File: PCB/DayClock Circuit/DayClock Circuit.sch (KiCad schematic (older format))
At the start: 42 parts, among them J10 Conn_02x08_Odd_Even, J11 Conn_01x02, J12 Conn_01x03, J13 Conn_01x03, J14 Stepper Motor, J3 molex 15-24-4441, J5 4002 LCD Screen, J6 Encoder, J7 RGB_LED_Strip_Connector, J8 RGB_LED_Strip_Connector, J9 RGB_LED_Strip_Connector, Q1 N-MOSFET, Q2 N-MOSFET, Q3 N-MOSFET, Q4 N-MOSFET, Q5 N-MOSFET, Q6 N-MOSFET, Q7 N-MOSFET, Q8 N-MOSFET, Q9 N-MOSFET, SW1 SW_DIP_x03, U1 Tiny_RTC_DS1307, U2 DRV8825_module

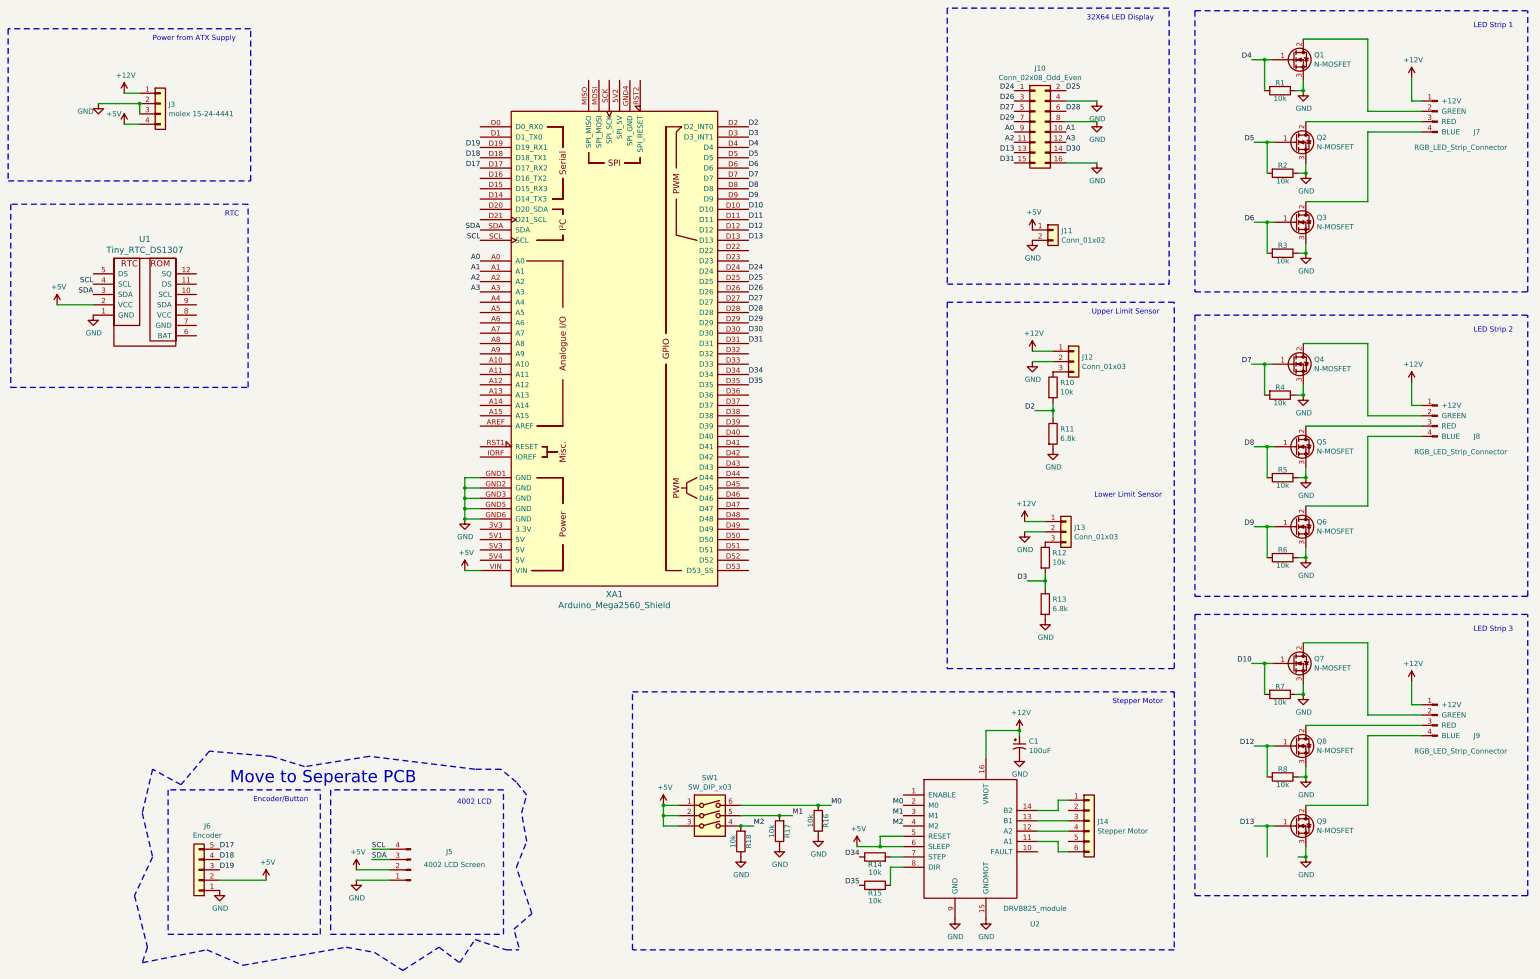
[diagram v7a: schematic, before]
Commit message: Split control box to a seperate PCB connected by a CAT5 cable. Schematic is complete, foot prints need to be finalized before layout.
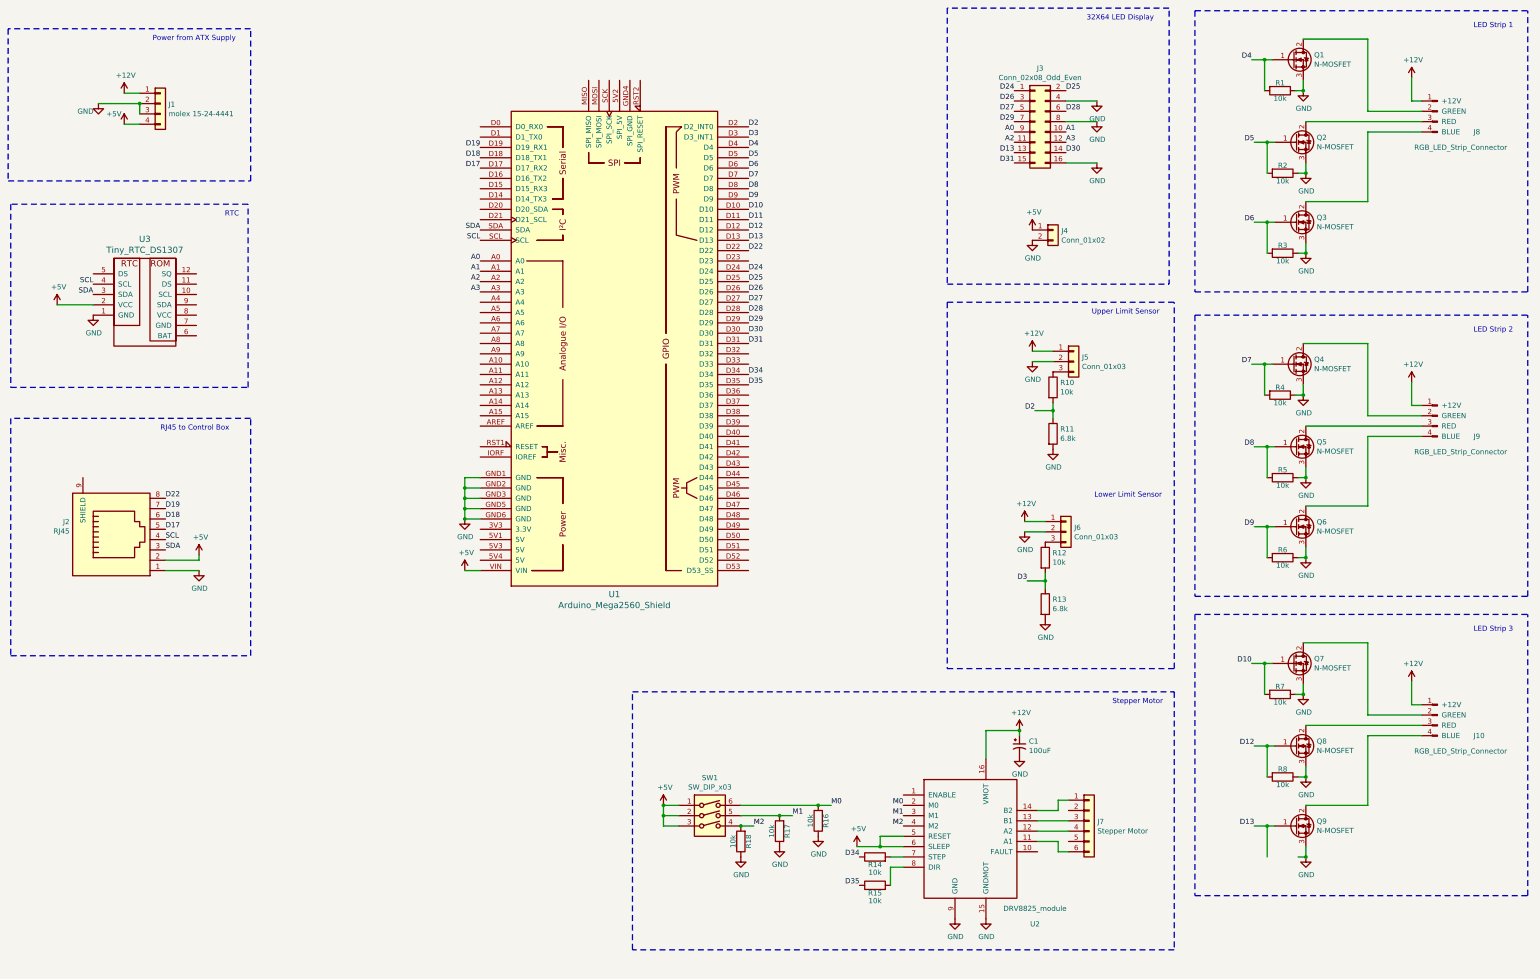
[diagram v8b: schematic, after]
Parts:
- removed J5: 4002 LCD Screen, Connectors_JST:JST_XH_B04B-XH-A_04x2.50mm_Straight, symbol Connector_Generic:Conn_01x04_Male
- removed J6: Encoder, Connector_JST:JST_XH_B05B-XH-A_1x05_P2.50mm_Vertical, symbol Connector_Generic:Conn_01x05
- added J2: RJ45, Connector_RJ:RJ45_Amphenol_RJHSE538X, symbol Connector_Specialized:RJ45
- C1: footprint (none) -> Capacitor_THT:CP_Radial_D6.3mm_P2.50mm
- renumbered J3 to J1, J9 to J10, J10 to J3, J11 to J4, J12 to J5, J13 to J6, J14 to J7, J7 to J8, J8 to J9, XA1 to U1, U1 to U3
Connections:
- net +5V: now also J2.2
- net D17: now also J2.5
- net D18: now also J2.6
- net D19: now also J2.7
- net GND: now also J2.1
- net SCL: now also J2.4
- net SDA: now also J2.3
- net D22: now reaches U1.D22
- net D22: now also J2.8
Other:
- note added: "RJ45 to Control Box"
- note removed: "4002 LCD"
- note removed: "Encoder/Button"
- note removed: "Move to Seperate PCB"
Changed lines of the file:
@@
 $EndDescr
 $Comp
-L rich_symbols:Tiny_RTC_DS1307 U1
+L rich_symbols:Tiny_RTC_DS1307 U3
 U 1 1 5A71AFB0
 P 2350 3625
-F 0 "U1" H 2350 4312 60  0000 C CNN
+F 0 "U3" H 2350 4312 60  0000 C CNN
 F 1 "Tiny_RTC_DS1307" H 2350 4206 60  0000 C CNN
 F 2 "rich-footprints:TinyRTC-one-mounting-hole" H 2400 3725 60  0001 C CNN
@@
 	1    0    0    -1
 $EndComp
-Text Label 4550 8850 0    50   ~ 0
-SCL
-Text Label 4550 8950 0    50   ~ 0
-SDA
-Wire Wire Line
-	4550 8850 4725 8850
-Wire Wire Line
-	4550 8950 4725 8950
 $Comp
 L power:+5V #PWR09
@@
 	1850 3575 1500 3575
 $Comp
-L power:GND #PWR013
-U 1 1 5A79A6E1
-P 3075 9250
-F 0 "#PWR013" H 3075 9000 50  0001 C CNN
-F 1 "GND" H 3080 9077 50  0000 C CNN
-F 2 "" H 3075 9250 50  0001 C CNN
-F 3 "" H 3075 9250 50  0001 C CNN
-	1    3075 9250
-	1    0    0    -1
-$EndComp
-$Comp
-L Connector_Generic:Conn_01x04_Male J5
-U 1 1 5AFFD786
-P 4925 9050
-F 0 "J5" H 4550 8875 50  0000 C CNN
-F 1 "4002 LCD Screen" H 4500 9000 50  0000 C CNN
-F 2 "Connectors_JST:JST_XH_B04B-XH-A_04x2.50mm_Straight" H 4925 9050 50  0001 C CNN
-F 3 "~" H 4925 9050 50  0001 C CNN
-	1    4925 9050
-	-1   0    0    1
-$EndComp
-$Comp
-L power:+5V #PWR0101
-U 1 1 5AFFEF10
-P 4400 9050
-F 0 "#PWR0101" H 4400 8900 50  0001 C CNN
-F 1 "+5V" H 4415 9223 50  0000 C CNN
-F 2 "" H 4400 9050 50  0001 C CNN
-F 3 "" H 4400 9050 50  0001 C CNN
-	1    4400 9050
-	1    0    0    -1
-$EndComp
-$Comp
-L power:GND #PWR0102
-U 1 1 5AFFEF2B
-P 4400 9150
-F 0 "#PWR0102" H 4400 8900 50  0001 C CNN
-F 1 "GND" H 4405 8977 50  0000 C CNN
-F 2 "" H 4400 9150 50  0001 C CNN
-F 3 "" H 4400 9150 50  0001 C CNN
-	1    4400 9150
-	1    0    0    -1
-$EndComp
-Wire Wire Line
-	4725 9150 4400 9150
-Wire Wire Line
-	4400 9050 4725 9050
-$Comp
-L Connector_Generic:Conn_01x05 J6
-U 1 1 5B03D90E
-P 2875 9050
-F 0 "J6" H 2795 8625 50  0000 C CNN
-F 1 "Encoder" H 2795 8716 50  0000 C CNN
-F 2 "Connector_JST:JST_XH_B05B-XH-A_1x05_P2.50mm_Vertical" H 2875 9050 50  0001 C CNN
-F 3 "~" H 2875 9050 50  0001 C CNN
-	1    2875 9050
-	-1   0    0    1
-$EndComp
-$Comp
-L power:+5V #PWR0103
-U 1 1 5B03DD9C
-P 3525 9150
-F 0 "#PWR0103" H 3525 9000 50  0001 C CNN
-F 1 "+5V" H 3540 9323 50  0000 C CNN
-F 2 "" H 3525 9150 50  0001 C CNN
-F 3 "" H 3525 9150 50  0001 C CNN
-	1    3525 9150
-	1    0    0    -1
-$EndComp
-Wire Wire Line
-	3075 9150 3525 9150
-$Comp
-L rich_symbols:RGB_LED_Strip_Connector J7
+L rich_symbols:RGB_LED_Strip_Connector J8
 U 1 1 5B09E233
 P 14825 1750
-F 0 "J7" H 15225 1600 50  0000 L CNN
+F 0 "J8" H 15225 1600 50  0000 L CNN
 F 1 "RGB_LED_Strip_Connector" H 14650 1450 50  0000 L CNN
 F 2 "Connector_JST:JST_XH_B04B-XH-A_1x04_P2.50mm_Vertical" H 14825 1750 50  0001 C CNN
@@
 LED Strip 1
 $Comp
-L rich_symbols:RGB_LED_Strip_Connector J8
+L rich_symbols:RGB_LED_Strip_Connector J9
 U 1 1 5B0C5230
 P 14825 4700
-F 0 "J8" H 15225 4550 50  0000 L CNN
+F 0 "J9" H 15225 4550 50  0000 L CNN
 F 1 "RGB_LED_Strip_Connector" H 14650 4400 50  0000 L CNN
 F 2 "Connector_JST:JST_XH_B04B-XH-A_1x04_P2.50mm_Vertical" H 14825 4700 50  0001 C CNN
@@
 LED Strip 2
 $Comp
-L rich_symbols:RGB_LED_Strip_Connector J9
+L rich_symbols:RGB_LED_Strip_Connector J10
 U 1 1 5B0C699D
 P 14825 7600
-F 0 "J9" H 15225 7450 50  0000 L CNN
+F 0 "J10" H 15225 7450 50  0000 L CNN
 F 1 "RGB_LED_Strip_Connector" H 14650 7300 50  0000 L CNN
 F 2 "Connector_JST:JST_XH_B04B-XH-A_1x04_P2.50mm_Vertical" H 14825 7600 50  0001 C CNN
@@
 LED Strip 3
 $Comp
-L Connector_Generic:Conn_02x08_Odd_Even J10
+L Connector_Generic:Conn_02x08_Odd_Even J3
 U 1 1 5B0E4FF2
 P 10975 1800
-F 0 "J10" H 11025 2317 50  0000 C CNN
+F 0 "J3" H 11025 2317 50  0000 C CNN
 F 1 "Conn_02x08_Odd_Even" H 11025 2226 50  0000 C CNN
 F 2 "Connector_PinHeader_2.54mm:PinHeader_2x08_P2.54mm_Vertical" H 10975 1800 50  0001 C CNN
@@
 	10125 3375 12275 3375
 $Comp
-L arduino:Arduino_Mega2560_Shield XA1
+L arduino:Arduino_Mega2560_Shield U1
 U 1 1 5B0E5F76
 P 6900 4000
-F 0 "XA1" H 6900 1620 60  0000 C CNN
+F 0 "U1" H 6900 1620 60  0000 C CNN
 F 1 "Arduino_Mega2560_Shield" H 6900 1514 60  0000 C CNN
 F 2 "Arduino:Arduino_Mega2560_Shield" H 7600 6750 60  0001 C CNN
@@
 $EndComp
 $Comp
-L Connector_Generic:Conn_01x02 J11
+L Connector_Generic:Conn_01x02 J4
 U 1 1 5B0E97EB
 P 11150 2850
-F 0 "J11" H 11230 2842 50  0000 L CNN
+F 0 "J4" H 11230 2842 50  0000 L CNN
 F 1 "Conn_01x02" H 11230 2751 50  0000 L CNN
 F 2 "TerminalBlock:TerminalBlock_Altech_AK300-2_P5.00mm" H 11150 2850 50  0001 C CNN
@@
 RTC
 $Comp
-L Connector_Generic:Conn_01x04 J3
+L Connector_Generic:Conn_01x04 J1
 U 1 1 5B13490E
 P 2500 1625
-F 0 "J3" H 2579 1617 50  0000 L CNN
+F 0 "J1" H 2579 1617 50  0000 L CNN
 F 1 "molex 15-24-4441" H 2579 1526 50  0000 L CNN
 F 2 "TerminalBlock_Phoenix:TerminalBlock_Phoenix_MKDS-1,5-4-5.08_1x04_P5.08mm_Horizontal" H 2500 1625 50  0001 C CNN
@@
 Text Notes 2425 1025 0    50   ~ 0
 Power from ATX Supply
-Wire Notes Line
-	5825 9675 5825 8275
-Wire Notes Line
-	5825 8275 4150 8275
-Wire Notes Line
-	4150 8275 4150 9675
-Wire Notes Line
-	4150 9675 5825 9675
-Text Notes 5375 8425 0    50   ~ 0
-4002 LCD
-Wire Notes Line
-	4050 9675 4050 8275
-Wire Notes Line
-	4050 8275 2575 8275
-Wire Notes Line
-	2575 8275 2575 9675
-Wire Notes Line
-	2575 9675 4050 9675
-Text Notes 3400 8400 0    50   ~ 0
-Encoder/Button
-Wire Notes Line
-	5975 9800 5925 9625
-Wire Notes Line
-	5925 9625 6100 9475
-Wire Notes Line
-	6100 9475 5950 9025
-Wire Notes Line
-	5950 9025 6050 8775
-Wire Notes Line
-	6050 8775 6000 8500
-Wire Notes Line
-	6000 8500 6050 8325
-Wire Notes Line
-	6050 8325 5950 8200
-Wire Notes Line
-	5950 8200 5800 8075
-Wire Notes Line
-	5800 8075 5550 8075
-Wire Notes Line
-	5550 8075 4525 7950
-Wire Notes Line
-	4525 7950 3900 8050
-Wire Notes Line
-	3575 7950 2975 7900
-Wire Notes Line
-	2975 7900 2700 8225
-Wire Notes Line
-	2700 8225 2425 8075
-Wire Notes Line
-	2425 8075 2325 8500
-Wire Notes Line
-	2325 8500 2425 8925
-Wire Notes Line
-	2425 8925 2250 9300
-Wire Notes Line
-	2250 9300 2375 9800
-Wire Notes Line
-	2375 9800 2325 9950
-Wire Notes Line
-	2325 9950 2950 9825
-Wire Notes Line
-	2950 9825 3300 9975
-Wire Notes Line
-	3300 9975 4300 9800
-Wire Notes Line
-	4300 9800 4575 9850
-Wire Notes Line
-	4575 9850 4850 10025
-Wire Notes Line
-	4850 10025 5200 9800
-Wire Notes Line
-	5200 9800 5400 9950
-Wire Notes Line
-	5400 9950 5550 9725
-Wire Notes Line
-	5550 9725 5850 9825
-Wire Notes Line
-	5850 9825 5975 9825
-Text Notes 3175 8225 0    118  ~ 0
-Move to Seperate PCB
-Wire Notes Line
-	3575 7950 3900 8050
-Text Label 3075 8850 0    50   ~ 0
+Text Label 2550 5750 0    50   ~ 0
 D17
-Text Label 3075 8950 0    50   ~ 0
+Text Label 2550 5650 0    50   ~ 0
 D18
-Text Label 3075 9050 0    50   ~ 0
+Text Label 2550 5550 0    50   ~ 0
 D19
 Text Label 5600 2250 2    50   ~ 0
@@
 D19
 $Comp
-L Connector_Generic:Conn_01x03 J12
+L Connector_Generic:Conn_01x03 J5
 U 1 1 5B10F747
 P 11350 4125
-F 0 "J12" H 11430 4167 50  0000 L CNN
+F 0 "J5" H 11430 4167 50  0000 L CNN
 F 1 "Conn_01x03" H 11430 4076 50  0000 L CNN
 F 2 "Connector_JST:JST_XH_B03B-XH-A_1x03_P2.50mm_Vertical" H 11350 4125 50  0001 C CNN
@@
 Upper Limit Sensor
 $Comp
-L Connector_Generic:Conn_01x03 J13
+L Connector_Generic:Conn_01x03 J6
 U 1 1 5B14EA09
 P 11275 5775
-F 0 "J13" H 11355 5817 50  0000 L CNN
+F 0 "J6" H 11355 5817 50  0000 L CNN
 F 1 "Conn_01x03" H 11355 5726 50  0000 L CNN
 F 2 "Connector_JST:JST_XH_B03B-XH-A_1x03_P2.50mm_Vertical" H 11275 5775 50  0001 C CNN
@@
 $EndComp
 $Comp
-L Connector_Generic:Conn_01x06 J14
+L Connector_Generic:Conn_01x06 J7
 U 1 1 5B169A57
 P 11500 8575
-F 0 "J14" H 11580 8567 50  0000 L CNN
+F 0 "J7" H 11580 8567 50  0000 L CNN
 F 1 "Stepper Motor" H 11580 8476 50  0000 L CNN
 F 2 "" H 11500 8575 50  0001 C CNN
@@
 F 0 "C1" H 10916 7896 50  0000 L CNN
 F 1 "100uF" H 10916 7805 50  0000 L CNN
-F 2 "" H 10825 7850 50  0001 C CNN
+F 2 "Capacitor_THT:CP_Radial_D6.3mm_P2.50mm" H 10825 7850 50  0001 C CNN
 F 3 "~" H 10825 7850 50  0001 C CNN
 	1    10825 7850
@@
 Wire Wire Line
 	9575 9025 9575 9200
+$Comp
+L Connector_Specialized:RJ45 J2
+U 1 1 5B12B8C7
+P 2100 5800
+F 0 "J2" V 2223 6280 50  0000 L CNN
+F 1 "RJ45" V 2132 6280 50  0000 L CNN
+F 2 "Connector_RJ:RJ45_Amphenol_RJHSE538X" H 2100 5800 50  0001 C CNN
+F 3 "" H 2100 5800 50  0001 C CNN
+	1    2100 5800
+	0    -1   -1   0
+$EndComp
+$Comp
+L power:GND #PWR0101
+U 1 1 5B145465
+P 2875 6150
+F 0 "#PWR0101" H 2875 5900 50  0001 C CNN
+F 1 "GND" H 2880 5977 50  0000 C CNN
+F 2 "" H 2875 6150 50  0001 C CNN
+F 3 "" H 2875 6150 50  0001 C CNN
+	1    2875 6150
+	1    0    0    -1
+$EndComp
+Wire Wire Line
+	2550 6150 2875 6150
+$Comp
+L power:+5V #PWR0102
+U 1 1 5B1525E1
+P 2875 6000
+F 0 "#PWR0102" H 2875 5850 50  0001 C CNN
+F 1 "+5V" H 2890 6173 50  0000 C CNN
+F 2 "" H 2875 6000 50  0001 C CNN
+F 3 "" H 2875 6000 50  0001 C CNN
+	1    2875 6000
+	1    0    0    -1
+$EndComp
+Wire Wire Line
+	2550 6050 2875 6050
+Wire Wire Line
+	2875 6050 2875 6000
+Text Label 2550 5950 0    50   ~ 0
+SDA
+Text Label 2550 5850 0    50   ~ 0
+SCL
+Text Label 8200 3050 0    50   ~ 0
+D22
+Text Label 2550 5450 0    50   ~ 0
+D22
+Wire Notes Line
+	1050 4675 1050 6975
+Wire Notes Line
+	1050 6975 3375 6975
+Wire Notes Line
+	3375 6975 3375 4675
+Wire Notes Line
+	3375 4675 1050 4675
+Text Notes 2500 4800 0    50   ~ 0
+RJ45 to Control Box
 $EndSCHEMATC
